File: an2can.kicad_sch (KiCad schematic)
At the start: 18 parts, among them J1 PWR/CAN, U1 MAX6025, U2 Tex_DCDC_v2

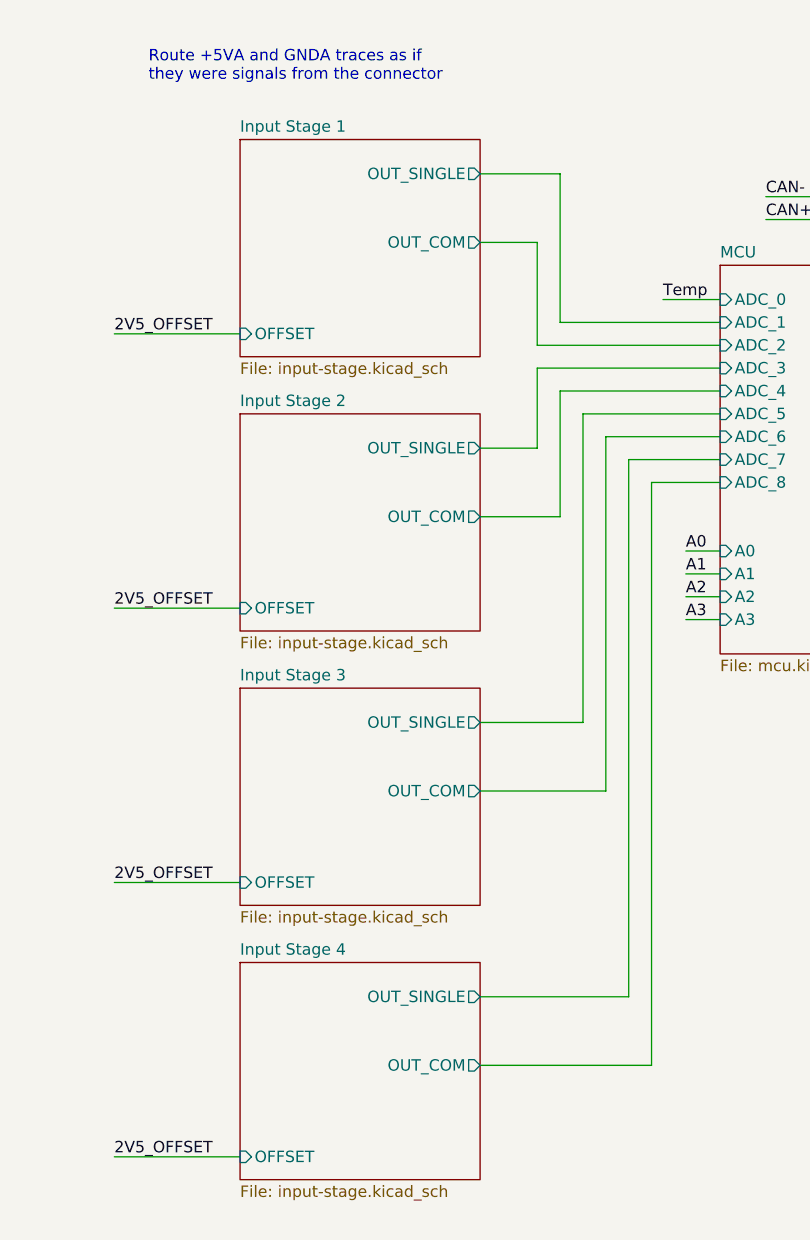
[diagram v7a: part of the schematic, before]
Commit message: pcb: finalize routing of analog section
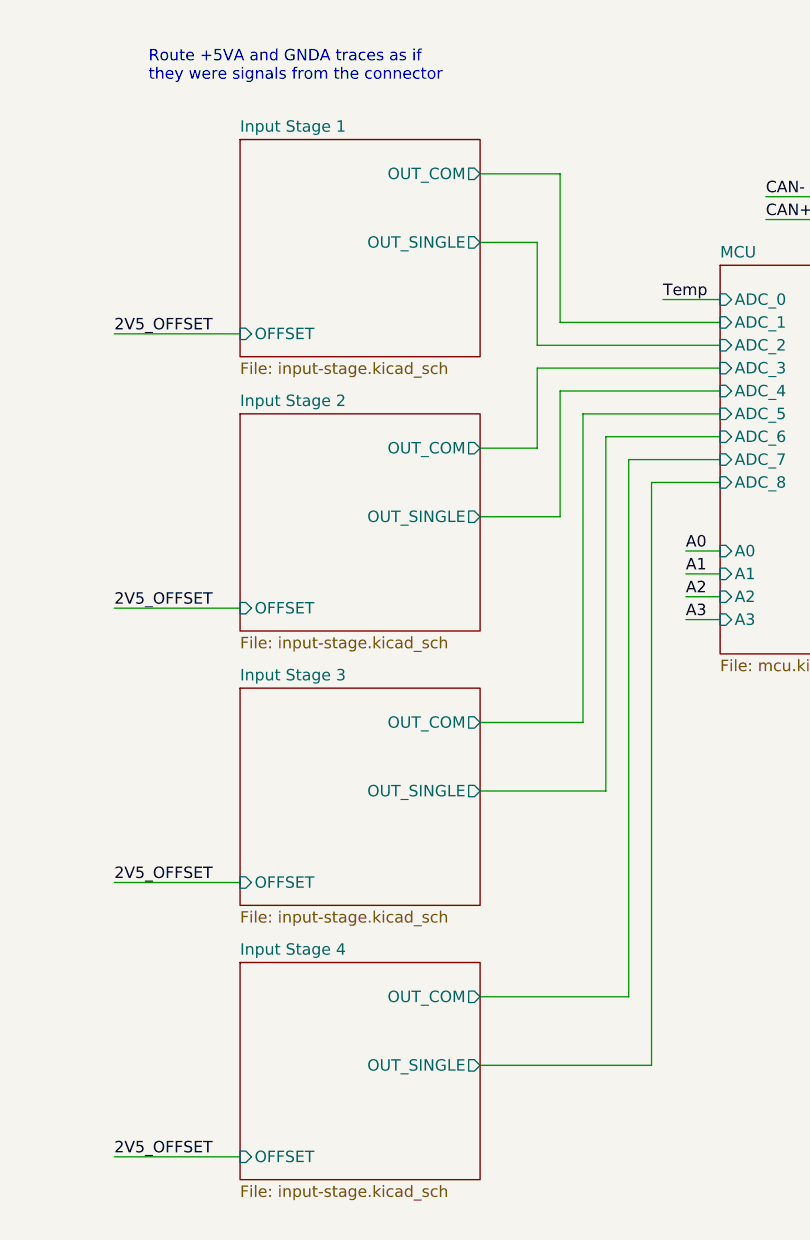
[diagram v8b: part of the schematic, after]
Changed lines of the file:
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@@
       (effects (font (size 1.27 1.27)) (justify left top))
     )
-    (pin "OUT_COM" output (at 185.42 134.62 0)
+    (pin "OUT_SINGLE" output (at 185.42 134.62 0)
       (effects (font (size 1.27 1.27)) (justify right))
     )
-    (pin "OUT_SINGLE" output (at 185.42 127 0)
+    (pin "OUT_COM" output (at 185.42 127 0)
       (effects (font (size 1.27 1.27)) (justify right))
     )
@@
       (effects (font (size 1.27 1.27)) (justify left top))
     )
-    (pin "OUT_COM" output (at 185.42 43.18 0)
+    (pin "OUT_SINGLE" output (at 185.42 43.18 0)
       (effects (font (size 1.27 1.27)) (justify right))
     )
-    (pin "OUT_SINGLE" output (at 185.42 35.56 0)
+    (pin "OUT_COM" output (at 185.42 35.56 0)
       (effects (font (size 1.27 1.27)) (justify right))
     )
@@
       (effects (font (size 1.27 1.27)) (justify left top))
     )
-    (pin "OUT_COM" output (at 185.42 73.66 0)
+    (pin "OUT_SINGLE" output (at 185.42 73.66 0)
       (effects (font (size 1.27 1.27)) (justify right))
     )
-    (pin "OUT_SINGLE" output (at 185.42 66.04 0)
+    (pin "OUT_COM" output (at 185.42 66.04 0)
       (effects (font (size 1.27 1.27)) (justify right))
     )
@@
       (effects (font (size 1.27 1.27)) (justify left top))
     )
-    (pin "OUT_COM" output (at 185.42 104.14 0)
+    (pin "OUT_SINGLE" output (at 185.42 104.14 0)
       (effects (font (size 1.27 1.27)) (justify right))
     )
-    (pin "OUT_SINGLE" output (at 185.42 96.52 0)
+    (pin "OUT_COM" output (at 185.42 96.52 0)
       (effects (font (size 1.27 1.27)) (justify right))
     )
